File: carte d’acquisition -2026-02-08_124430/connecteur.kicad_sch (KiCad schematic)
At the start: 1 part, among them J2 Conn_02x05_Counter_Clockwise

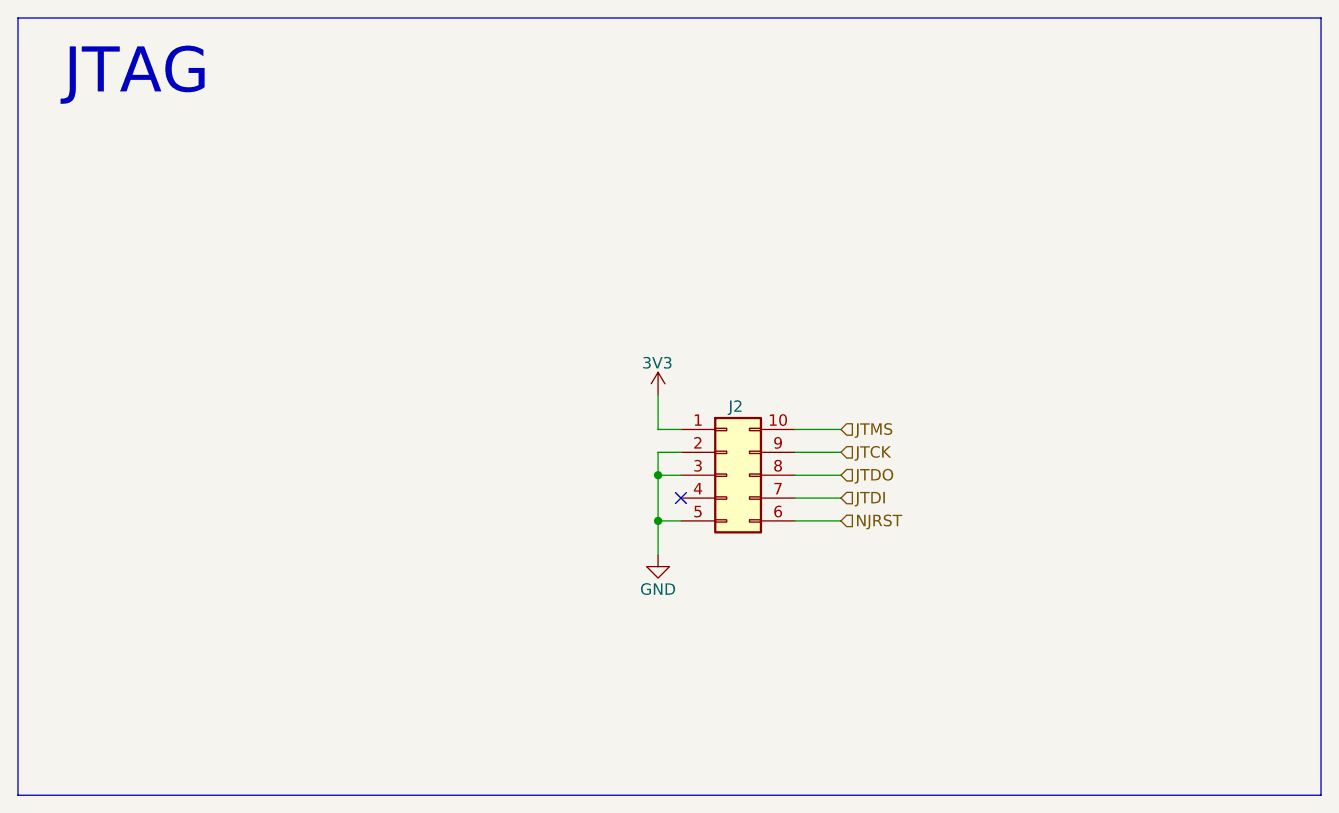
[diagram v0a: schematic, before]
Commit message: Mis a jour plusieurs circuit et ajouter beaucoup de footprint manquant
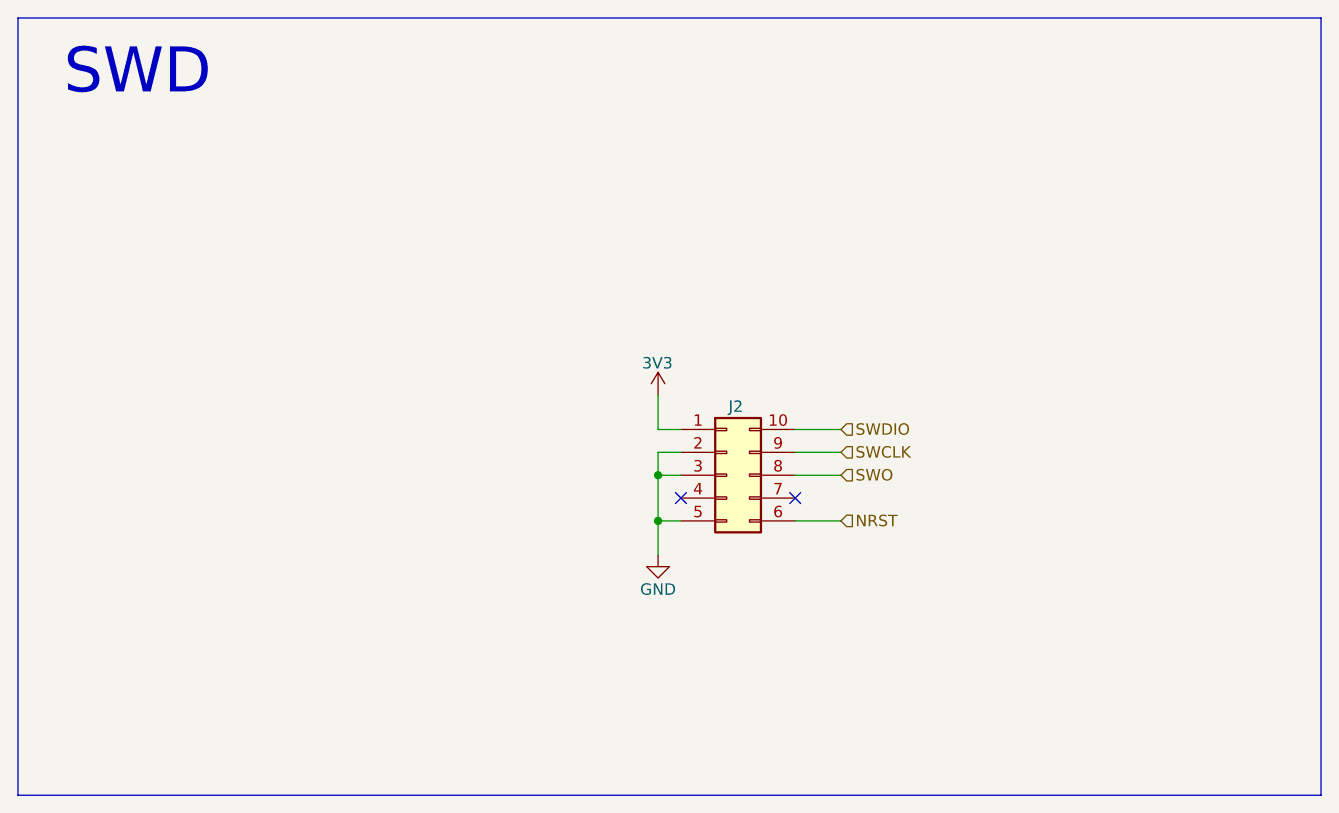
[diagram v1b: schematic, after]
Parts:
- J2: footprint (none) -> Connector_PinSocket_2.00mm:PinSocket_2x05_P2.00mm_Vertical
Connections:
- net JTCK renamed SWCLK
- net JTDI: no longer names the net of J2.7 (Pin_7)
- net JTDO renamed SWO
- net JTMS renamed SWDIO
- net NJRST renamed NRST
- no-connect marks 1 -> 2
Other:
- note added: "SWD"
- note removed: "JTAG"
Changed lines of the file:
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@@
 		)
 	)
-	(text "JTAG\n"
+	(text "SWD"
 		(exclude_from_sim no)
 		(at 74.93 50.546 0)
@@
 		(at 143.51 97.79)
 	)
+	(no_connect
+		(at 156.21 97.79)
+	)
 	(wire
 		(pts
@@
 	(wire
 		(pts
-			(xy 156.21 97.79) (xy 161.29 97.79)
-		)
-		(stroke
-			(width 0)
-			(type default)
-		)
-	)
-	(wire
-		(pts
 			(xy 140.97 95.25) (xy 140.97 100.33)
 		)
@@
 		)
 	)
-	(hierarchical_label "JTDO"
+	(hierarchical_label "SWO"
 		(shape input)
 		(at 161.29 95.25 0)
@@
 		)
 	)
-	(hierarchical_label "JTCK"
+	(hierarchical_label "SWCLK"
 		(shape input)
 		(at 161.29 92.71 0)
@@
 		)
 	)
-	(hierarchical_label "NJRST"
+	(hierarchical_label "NRST"
 		(shape input)
 		(at 161.29 100.33 0)
@@
 		)
 	)
-	(hierarchical_label "JTDI"
-		(shape input)
-		(at 161.29 97.79 0)
-		(effects
-			(font
-				(size 1.27 1.27)
-			)
-			(justify left)
-		)
-	)
-	(hierarchical_label "JTMS"
+	(hierarchical_label "SWDIO"
 		(shape input)
 		(at 161.29 90.17 0)
@@
 			)
 		)
-		(property "Footprint" ""
+		(property "Footprint" "Connector_PinSocket_2.00mm:PinSocket_2x05_P2.00mm_Vertical"
 			(at 148.59 95.25 0)
 			(effects
